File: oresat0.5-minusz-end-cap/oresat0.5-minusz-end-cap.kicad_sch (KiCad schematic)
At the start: 35 parts, among them J2 U.FL-R-SMA, U1 LTC4305, U2 MMC5983MA, U3 MMC5983MA

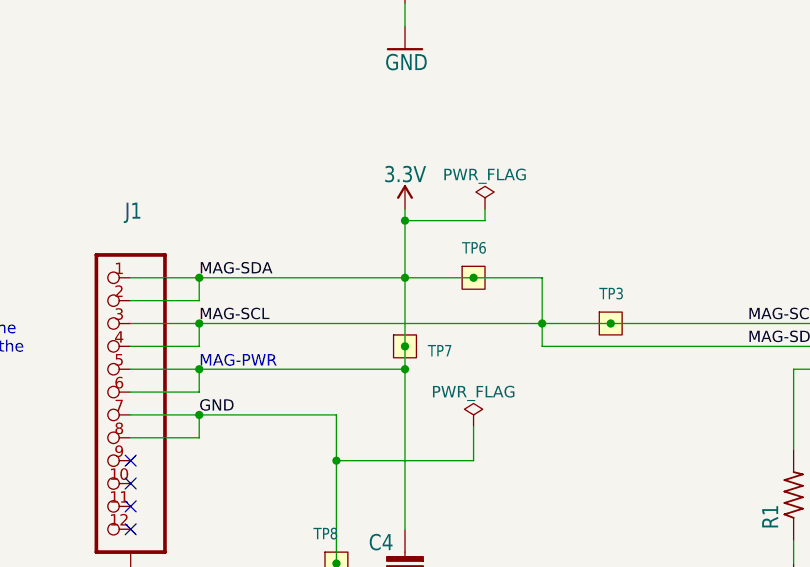
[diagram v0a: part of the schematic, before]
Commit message: moved endcap harwin connectors on both +/-Z endcaps per move in Onshape
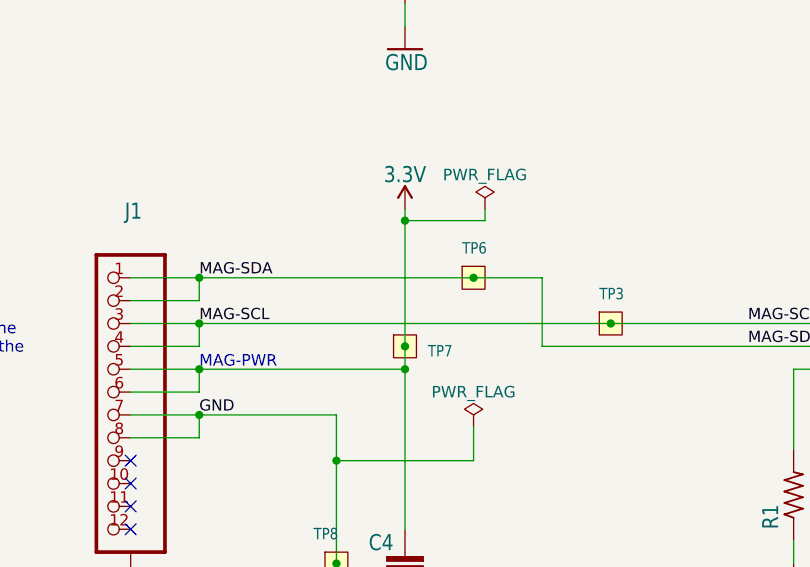
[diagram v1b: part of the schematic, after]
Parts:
- C1, C10, C12, C13, C2, C3, C4, C7, D2, J1, R1, R10, R2, R3, R4, R5, R6, R7, R8, R9: value (none) -> ~
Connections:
- net 3.3V: no longer J1.1, J1.2, J1.3, J1.4, TP3.1, TP6.1, U1.3 (SDAIN), U1.5 (SCLIN)
- new net MAG-SCL: J1.3, J1.4, TP3.1, U1.5 (SCLIN)
- new net MAG-SDA: J1.1, J1.2, TP6.1, U1.3 (SDAIN)
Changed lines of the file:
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@@
 	)
 	(junction
-		(at 124.46 111.76)
-		(diameter 0)
-		(color 0 0 0 0)
-	)
-	(junction
-		(at 139.7 116.84)
-		(diameter 0)
-		(color 0 0 0 0)
-	)
-	(junction
 		(at 233.68 96.52)
 		(diameter 0)
@@
 	(wire
 		(pts
-			(xy 139.7 116.84) (xy 101.6 116.84)
-		)
-		(stroke
-			(width 0)
-			(type default)
-		)
-	)
-	(wire
-		(pts
 			(xy 231.14 114.3) (xy 208.28 114.3)
 		)
@@
 	(wire
 		(pts
-			(xy 124.46 111.76) (xy 132.08 111.76)
+			(xy 101.6 111.76) (xy 132.08 111.76)
 		)
 		(stroke
@@
 	(wire
 		(pts
-			(xy 124.46 111.76) (xy 124.46 119.38)
-		)
-		(stroke
-			(width 0)
-			(type default)
-		)
-	)
-	(wire
-		(pts
 			(xy 231.14 161.29) (xy 231.14 158.75)
 		)
@@
 	(wire
 		(pts
-			(xy 139.7 116.84) (xy 147.32 116.84)
+			(xy 101.6 116.84) (xy 147.32 116.84)
 		)
 		(stroke
@@
 	(wire
 		(pts
-			(xy 124.46 105.41) (xy 124.46 111.76)
+			(xy 124.46 105.41) (xy 124.46 119.38)
 		)
 		(stroke
@@
 	(wire
 		(pts
-			(xy 139.7 116.84) (xy 139.7 111.76)
+			(xy 139.7 111.76) (xy 139.7 119.38)
 		)
 		(stroke
@@
 	(wire
 		(pts
-			(xy 139.7 119.38) (xy 139.7 116.84)
-		)
-		(stroke
-			(width 0)
-			(type default)
-		)
-	)
-	(wire
-		(pts
 			(xy 280.67 181.61) (xy 264.16 181.61)
 		)
@@
 	(wire
 		(pts
-			(xy 124.46 111.76) (xy 101.6 111.76)
-		)
-		(stroke
-			(width 0)
-			(type default)
-		)
-	)
-	(wire
-		(pts
 			(xy 233.68 96.52) (xy 236.22 96.52)
 		)
@@
 			)
 		)
-		(property "Value" ""
+		(property "Value" "~"
 			(at 325.12 120.65 0)
 			(effects
@@
 			)
 		)
-		(property "Value" ""
+		(property "Value" "~"
 			(at 91.44 124.46 0)
 			(effects
@@
 			)
 		)
-		(property "Value" ""
+		(property "Value" "~"
 			(at 236.22 104.14 0)
 			(effects
@@
 			)
 		)
-		(property "Value" ""
+		(property "Value" "~"
 			(at 236.22 166.37 0)
 			(effects
@@
 			)
 		)
-		(property "Value" ""
+		(property "Value" "~"
 			(at 231.14 104.14 0)
 			(effects
@@
 			)
 		)
-		(property "Value" ""
+		(property "Value" "~"
 			(at 175.26 104.14 0)
 			(effects
@@
 			)
 		)
-		(property "Value" ""
+		(property "Value" "~"
 			(at 210.82 104.14 0)
 			(effects
@@
 			)
 		)
-		(property "Value" ""
+		(property "Value" "~"
 			(at 231.14 166.37 0)
 			(effects
@@
 			)
 		)
-		(property "Value" ""
+		(property "Value" "~"
 			(at 275.59 153.67 0)
 			(effects
@@
 			)
 		)
-		(property "Value" ""
+		(property "Value" "~"
 			(at 198.12 96.52 0)
 			(effects
@@
 			)
 		)
-		(property "Value" ""
+		(property "Value" "~"
 			(at 167.64 135.89 0)
 			(effects
@@
 			)
 		)
-		(property "Value" ""
+		(property "Value" "~"
 			(at 215.9 104.14 0)
 			(effects
@@
 			)
 		)
-		(property "Value" ""
+		(property "Value" "~"
 			(at 325.12 91.44 0)
 			(effects
@@
 			)
 		)
-		(property "Value" ""
+		(property "Value" "~"
 			(at 124.46 142.24 0)
 			(effects
@@
 			)
 		)
-		(property "Value" ""
+		(property "Value" "~"
 			(at 275.59 91.44 0)
 			(effects
@@
 			)
 		)
-		(property "Value" ""
+		(property "Value" "~"
 			(at 121.92 173.99 0)
 			(effects
@@
 			)
 		)
-		(property "Value" ""
+		(property "Value" "~"
 			(at 325.12 153.67 0)
 			(effects
@@
 			)
 		)
-		(property "Value" ""
+		(property "Value" "~"
 			(at 325.12 182.88 0)
 			(effects
@@
 			)
 		)
-		(property "Value" ""
+		(property "Value" "~"
 			(at 121.92 184.15 90)
 			(effects
@@
 			)
 		)
-		(property "Value" ""
+		(property "Value" "~"
 			(at 210.82 137.16 0)
 			(effects

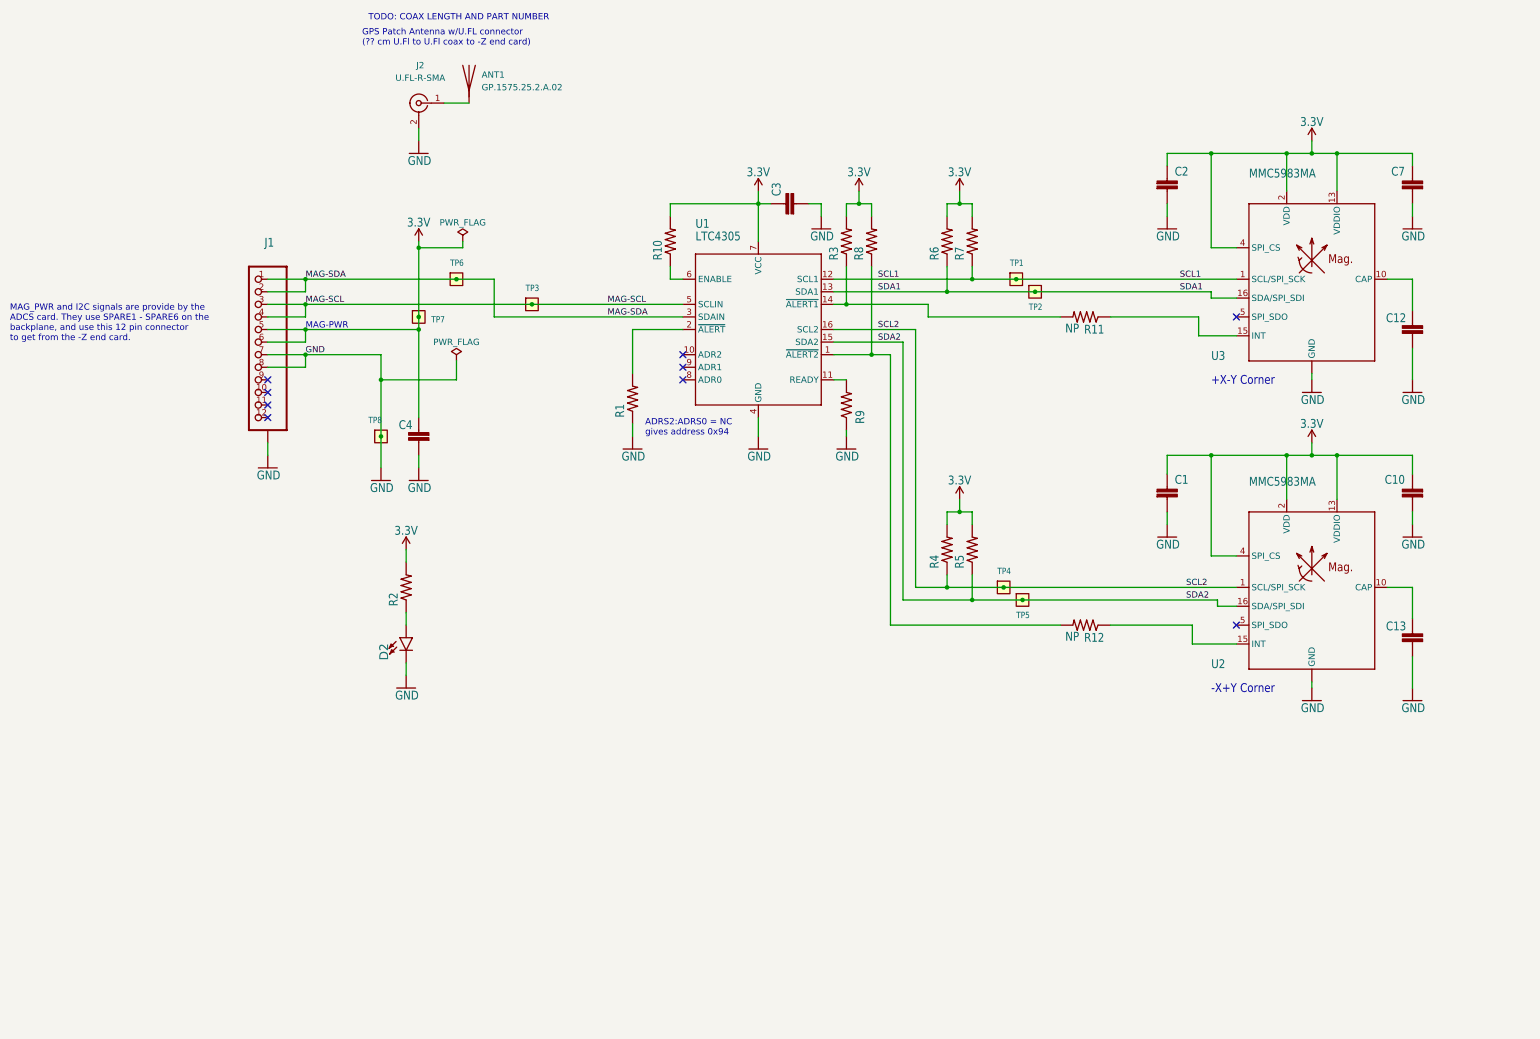
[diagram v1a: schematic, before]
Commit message: OreSat 0.5 Endcaps (+Z v1.3 and -Z v1.2) ready for ordering, reviewed -Z endcap, made small library and neatness changes to +Z endcap
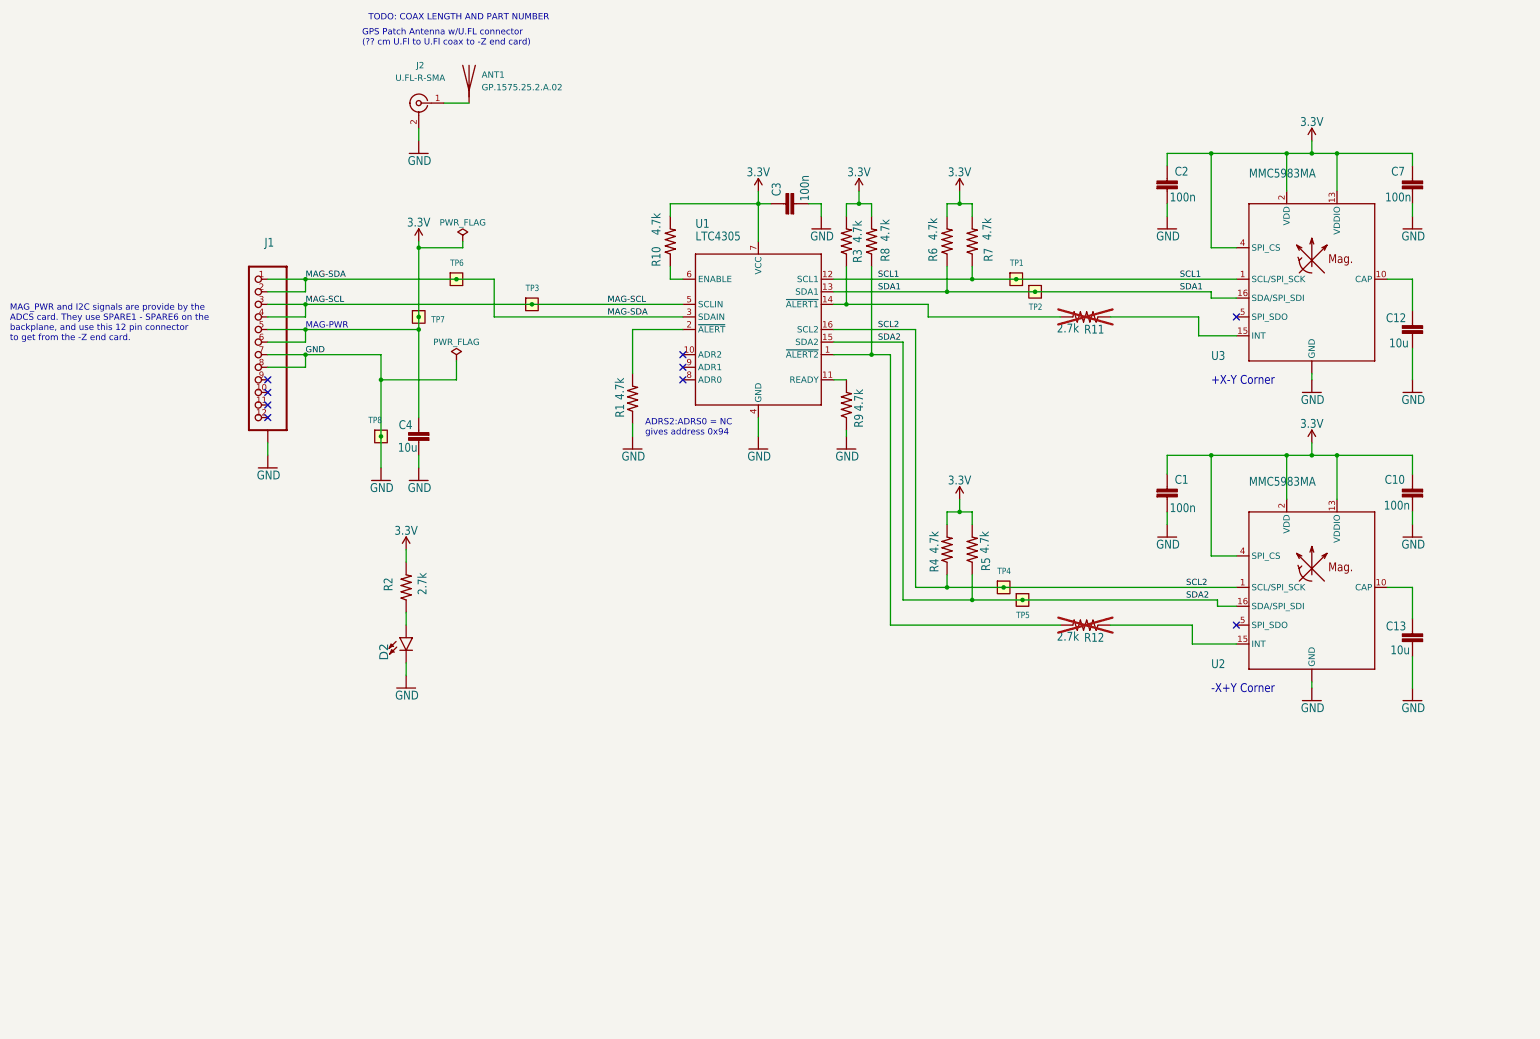
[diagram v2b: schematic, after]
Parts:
- C1, C10, C2, C3, C7: value ~ -> 100n
- C12, C13, C4: value ~ -> 10u
- R1, R10, R3, R4, R5, R6, R7, R8, R9: value ~ -> 4.7k
- R11, R12: value NP -> 2.7k; now not fitted
- R2: value ~ -> 2.7k
- U1: footprint oresat0-plusz-end-cap:16-SSOP -> oresat-ics:16-SSOP
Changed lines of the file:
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@@
 			)
 		)
-		(property "Value" "~"
-			(at 325.12 120.65 0)
+		(property "Value" "10u"
+			(at 324.358 125.73 0)
 			(effects
 				(font
@@
 				)
 				(justify left bottom)
-				(hide yes)
 			)
 		)
@@
 	)
 	(symbol
-		(lib_name "MMC5983MA_1")
 		(lib_id "oresat-ics:MMC5983MA")
 		(at 304.8 111.76 0)
@@
 		(in_bom yes)
 		(on_board yes)
-		(dnp no)
+		(dnp yes)
 		(property "Reference" "R12"
 			(at 262.89 183.1086 0)
@@
 			)
 		)
-		(property "Value" "NP"
+		(property "Value" "2.7k"
 			(at 257.81 182.88 0)
 			(effects
@@
 			)
 		)
-		(property "Footprint" "oresat0-plusz-end-cap:16-SSOP"
+		(property "Footprint" "oresat-ics:16-SSOP"
 			(at 193.04 87.63 0)
 			(effects
@@
 		(dnp no)
 		(property "Reference" "R7"
-			(at 234.7214 107.95 0)
+			(at 240.538 108.204 0)
 			(effects
 				(font
@@
 			)
 		)
-		(property "Value" "~"
-			(at 236.22 104.14 0)
+		(property "Value" "4.7k"
+			(at 240.284 103.886 0)
 			(effects
 				(font
@@
 				)
 				(justify left bottom)
-				(hide yes)
 			)
 		)
@@
 		(dnp no)
 		(property "Reference" "R5"
-			(at 234.7214 170.18 0)
+			(at 240.03 170.688 0)
 			(effects
 				(font
@@
 			)
 		)
-		(property "Value" "~"
-			(at 236.22 166.37 0)
+		(property "Value" "4.7k"
+			(at 239.776 167.132 0)
 			(effects
 				(font
@@
 				)
 				(justify left bottom)
-				(hide yes)
 			)
 		)
@@
 		(dnp no)
 		(property "Reference" "R6"
-			(at 229.6414 107.95 0)
+			(at 229.362 108.204 0)
 			(effects
 				(font
@@
 			)
 		)
-		(property "Value" "~"
-			(at 231.14 104.14 0)
+		(property "Value" "4.7k"
+			(at 229.362 103.886 0)
 			(effects
 				(font
@@
 				)
 				(justify left bottom)
-				(hide yes)
 			)
 		)
@@
 		(dnp no)
 		(property "Reference" "R10"
-			(at 173.7614 107.95 0)
+			(at 173.482 109.22 0)
 			(effects
 				(font
@@
 			)
 		)
-		(property "Value" "~"
-			(at 175.26 104.14 0)
+		(property "Value" "4.7k"
+			(at 173.482 102.87 0)
 			(effects
 				(font
@@
 				)
 				(justify left bottom)
-				(hide yes)
 			)
 		)
@@
 		(dnp no)
 		(property "Reference" "R3"
-			(at 209.3214 107.95 0)
+			(at 214.122 108.458 0)
 			(effects
 				(font
@@
 			)
 		)
-		(property "Value" "~"
-			(at 210.82 104.14 0)
+		(property "Value" "4.7k"
+			(at 214.122 104.394 0)
 			(effects
 				(font
@@
 				)
 				(justify left bottom)
-				(hide yes)
 			)
 		)
@@
 		(dnp no)
 		(property "Reference" "R4"
-			(at 229.6414 170.18 0)
+			(at 229.616 170.942 0)
 			(effects
 				(font
@@
 			)
 		)
-		(property "Value" "~"
-			(at 231.14 166.37 0)
+		(property "Value" "4.7k"
+			(at 229.616 167.132 0)
 			(effects
 				(font
@@
 				)
 				(justify left bottom)
-				(hide yes)
 			)
 		)
@@
 			)
 		)
-		(property "Value" "~"
-			(at 275.59 153.67 0)
+		(property "Value" "100n"
+			(at 276.098 159.004 0)
 			(effects
 				(font
@@
 				)
 				(justify left bottom)
-				(hide yes)
 			)
 		)
@@
 		(in_bom yes)
 		(on_board yes)
-		(dnp no)
+		(dnp yes)
 		(property "Reference" "R11"
 			(at 262.89 120.8786 0)
@@
 			)
 		)
-		(property "Value" "NP"
+		(property "Value" "2.7k"
 			(at 257.81 120.65 0)
 			(effects
@@
 			)
 		)
-		(property "Value" "~"
-			(at 198.12 96.52 0)
+		(property "Value" "100n"
+			(at 203.454 96.012 0)
 			(effects
 				(font
@@
 				)
 				(justify left bottom)
-				(hide yes)
 			)
 		)
@@
 			)
 		)
-		(property "Description" ""
+		(property "Description" "Special symbol for telling ERC where power comes from"
 			(at 132.08 128.27 0)
 			(effects
@@
 			)
 		)
-		(property "Description" ""
+		(property "Description" "Special symbol for telling ERC where power comes from"
 			(at 133.35 104.14 0)
 			(effects
@@
 			)
 		)
-		(property "Value" "~"
-			(at 167.64 135.89 0)
+		(property "Value" "4.7k"
+			(at 166.116 136.144 0)
 			(effects
 				(font
@@
 				)
 				(justify left bottom)
-				(hide yes)
 			)
 		)
@@
 		(dnp no)
 		(property "Reference" "R8"
-			(at 214.4014 107.95 0)
+			(at 219.71 108.204 0)
 			(effects
 				(font
@@
 			)
 		)
-		(property "Value" "~"
-			(at 215.9 104.14 0)
+		(property "Value" "4.7k"
+			(at 219.71 104.14 0)
 			(effects
 				(font
@@
 				)
 				(justify left bottom)
-				(hide yes)
 			)
 		)
@@
 			)
 		)
-		(property "Value" "~"
-			(at 325.12 91.44 0)
+		(property "Value" "100n"
+			(at 324.866 96.266 0)
 			(effects
 				(font
@@
 				)
 				(justify left bottom)
-				(hide yes)
 			)
 		)
@@
 			)
 		)
-		(property "Value" "~"
-			(at 124.46 142.24 0)
+		(property "Value" "10u"
+			(at 124.206 146.812 0)
 			(effects
 				(font
@@
 				)
 				(justify left bottom)
-				(hide yes)
 			)
 		)
@@
 			)
 		)
-		(property "Value" "~"
-			(at 275.59 91.44 0)
+		(property "Value" "100n"
+			(at 276.098 96.266 0)
 			(effects
 				(font
@@
 				)
 				(justify left bottom)
-				(hide yes)
 			)
 		)
@@
 		(dnp no)
 		(property "Reference" "R2"
-			(at 120.4214 177.8 0)
+			(at 119.38 174.752 0)
 			(effects
 				(font
@@
 			)
 		)
-		(property "Value" "~"
-			(at 121.92 173.99 0)
+		(property "Value" "2.7k"
+			(at 126.238 175.514 0)
 			(effects
 				(font
@@
 				)
 				(justify left bottom)
-				(hide yes)
 			)
 		)
@@
 			)
 		)
-		(property "Value" "~"
-			(at 325.12 153.67 0)
+		(property "Value" "100n"
+			(at 324.612 158.496 0)
 			(effects
 				(font
@@
 				)
 				(justify left bottom)
-				(hide yes)
 			)
 		)
@@
 			)
 		)
-		(property "Value" "~"
-			(at 325.12 182.88 0)
+		(property "Value" "10u"
+			(at 324.612 187.706 0)
 			(effects
 				(font
@@
 				)
 				(justify left bottom)
-				(hide yes)
 			)
 		)
@@
 			)
 		)
-		(property "Description" ""
+		(property "Description" "coaxial connector (BNC, SMA, SMB, SMC, Cinch/RCA, LEMO, ...)"
 			(at 124.46 76.2 0)
 			(effects
@@
 		(dnp no)
 		(property "Reference" "R9"
-			(at 214.63 140.97 0)
+			(at 214.376 141.732 0)
 			(effects
 				(font
@@
 			)
 		)
-		(property "Value" "~"
-			(at 210.82 137.16 0)
+		(property "Value" "4.7k"
+			(at 214.376 138.43 0)
 			(effects
 				(font
@@
 				)
 				(justify left bottom)
-				(hide yes)
 			)
 		)

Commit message: Fixed issues 5 and 6 -- weird 4.7k values everywhere, missing libraries, and used no-place to indicate actual no place components.
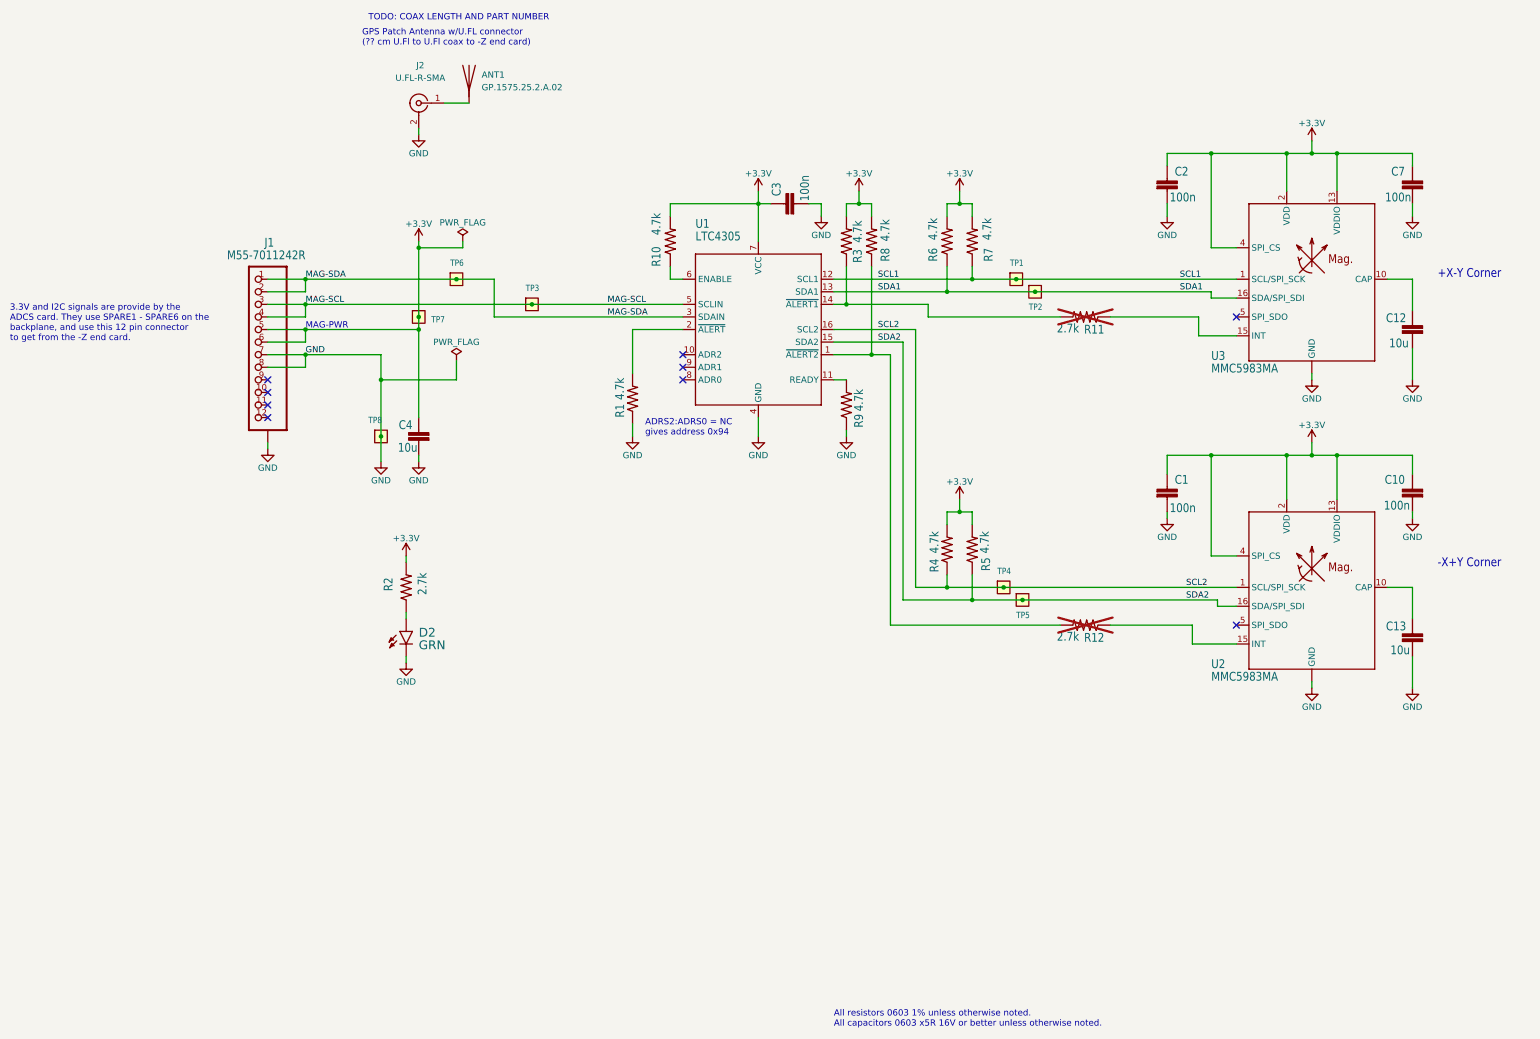
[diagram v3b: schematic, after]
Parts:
- D2: value ~ -> GRN
- J1: value ~ -> M55-7011242R
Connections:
- net 3.3V renamed +3.3V
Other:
- note added: "3.3V and I2C signals are provide by the ADCS card. They use SPARE1 - SPARE6 on the backplane, and use this 12 pin connector to get from the -Z end card."
- note added: "All resistors 0603 1% unless otherwise noted. All capacitors 0603 x5R 16V or better unless otherwise noted."
- note removed: "MAG_PWR and I2C signals are provide by the ADCS card. They use SPARE1 - SPARE6 on the backplane, and use this 12 pin connector to get from the -Z end card."
- moved on the sheet: D2
